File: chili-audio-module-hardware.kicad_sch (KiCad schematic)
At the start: 7 parts, among them J1 Conn_01x04_Pin, J2 Conn_01x02_Pin, J3 Conn_01x02_Pin, U1 MAX98357A

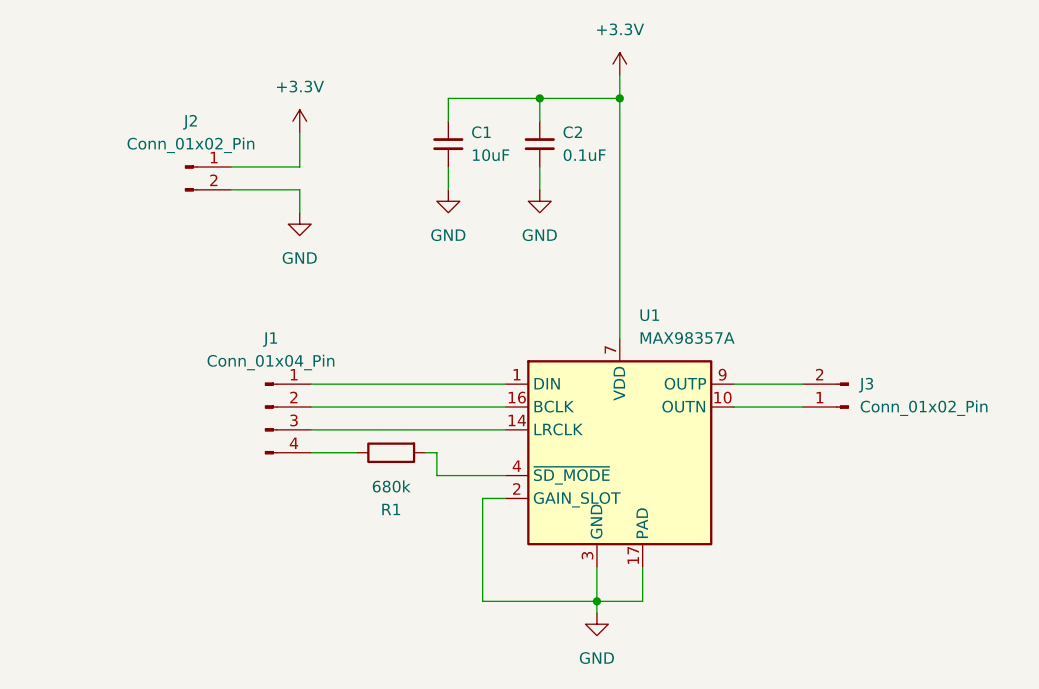
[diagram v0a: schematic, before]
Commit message: schematic finished with parts chosen
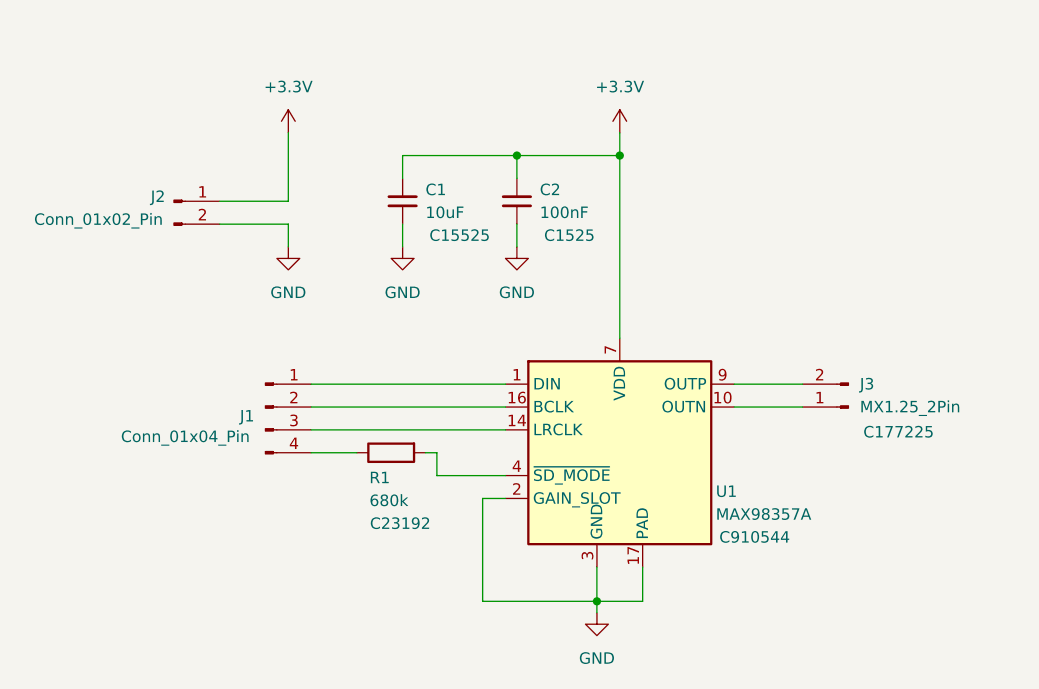
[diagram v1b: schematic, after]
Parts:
- C1: footprint Capacitor_SMD:C_0805_2012Metric -> Capacitor_SMD:C_0402_1005Metric; LCSC (none) -> C15525
- C2: value 0.1uF -> 100nF; footprint Capacitor_SMD:C_0603_1608Metric -> Capacitor_SMD:C_0402_1005Metric; LCSC (none) -> C1525
- J3: value Conn_01x02_Pin -> MX1.25_2Pin; LCSC (none) -> C177225
- R1: LCSC (none) -> C23192
- U1: LCSC (none) -> C910544
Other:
- moved on the sheet: C1, C2, J2

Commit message: pcb design
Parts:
- R1: value 680k -> 510k
- U1: footprint Package_DFN_QFN:TQFN-16-1EP_3x3mm_P0.5mm_EP1.23x1.23mm -> Package_DFN_QFN:TQFN-16-1EP_3x3mm_P0.5mm_EP1.23x1.23mm_ThermalVias
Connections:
- net at U1.10 (OUTN): now also J3.2 (Pin_2); no longer J3.1 (Pin_1)
- net at U1.9 (OUTP): now also J3.1 (Pin_1); no longer J3.2 (Pin_2)
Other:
- moved on the sheet: J3
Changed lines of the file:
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@@
+	(wire
+		(pts
+			(xy 168.91 88.9) (xy 176.53 88.9)
+		)
+		(stroke
+			(width 0)
+			(type default)
+		)
+	)
 	(wire
 		(pts
@@
 	(wire
 		(pts
+			(xy 168.91 91.44) (xy 176.53 91.44)
+		)
+		(stroke
+			(width 0)
+			(type default)
+		)
+	)
+	(wire
+		(pts
 			(xy 121.92 93.98) (xy 143.51 93.98)
 		)
@@
 	(wire
 		(pts
-			(xy 168.91 91.44) (xy 176.53 91.44)
-		)
-		(stroke
-			(width 0)
-			(type default)
-		)
-	)
-	(wire
-		(pts
 			(xy 132.08 66.04) (xy 132.08 63.5)
 		)
@@
 		(pts
 			(xy 135.89 99.06) (xy 143.51 99.06)
-		)
-		(stroke
-			(width 0)
-			(type default)
-		)
-	)
-	(wire
-		(pts
-			(xy 168.91 88.9) (xy 176.53 88.9)
 		)
 		(stroke
@@
 			)
 		)
-		(property "Footprint" "Package_DFN_QFN:TQFN-16-1EP_3x3mm_P0.5mm_EP1.23x1.23mm"
+		(property "Footprint" "Package_DFN_QFN:TQFN-16-1EP_3x3mm_P0.5mm_EP1.23x1.23mm_ThermalVias"
 			(at 154.94 99.06 0)
 			(hide yes)
@@
 			)
 		)
-		(property "Value" "680k"
+		(property "Value" "510k"
 			(at 130.556 101.854 90)
 			(show_name no)
@@
 	(symbol
 		(lib_id "Connector:Conn_01x02_Pin")
-		(at 181.61 91.44 180)
+		(at 181.61 88.9 0)
+		(mirror y)
 		(unit 1)
 		(body_style 1)
@@
 		(dnp no)
 		(property "Reference" "J3"
-			(at 182.88 88.8999 0)
+			(at 182.372 86.1061 0)
 			(show_name no)
 			(do_not_autoplace no)
@@
 		)
 		(property "Value" "MX1.25_2Pin"
-			(at 182.88 91.4399 0)
+			(at 182.372 88.646 0)
 			(show_name no)
 			(do_not_autoplace no)
@@
 		)
 		(property "Footprint" "Connector_Molex:Molex_PicoBlade_53261-0271_1x02-1MP_P1.25mm_Horizontal"
-			(at 181.61 91.44 0)
+			(at 181.61 88.9 0)
 			(hide yes)
 			(show_name no)
@@
 		)
 		(property "Datasheet" ""
-			(at 181.61 91.44 0)
+			(at 181.61 88.9 0)
 			(hide yes)
 			(show_name no)
@@
 		)
 		(property "Description" "Generic connector, single row, 01x02, script generated"
-			(at 181.61 91.44 0)
+			(at 181.61 88.9 0)
 			(hide yes)
 			(show_name no)
@@
 		)
 		(property "LCSC" "C177225"
-			(at 187.198 94.234 0)
-			(show_name no)
-			(do_not_autoplace no)
+			(at 186.69 91.186 0)
+			(show_name no)
+			(do_not_autoplace no)
